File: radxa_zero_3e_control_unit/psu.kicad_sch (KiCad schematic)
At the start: 17 parts, among them J1 USB STM32, J11 ETH_IN, J12 ETH_OUT, J2 DC IN, U1 TPS54202DDC, U4 DCDC_MP2315, U7 PoE->24V

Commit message: Various
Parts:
- added J26, J27: IO, Connector_JST:JST_XH_B6B-XH-A_1x06_P2.50mm_Vertical, symbol Connector_Generic:Conn_01x06
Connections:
- net +5V: now also J27.5 (Pin_5), J27.6 (Pin_6)
- net +9V: now also J27.1 (Pin_1), J27.2 (Pin_2)
- net 5-24V: now also J2.1, J26.1 (Pin_1), J26.2 (Pin_2), J26.3 (Pin_3); no longer J2.2
- net GND: now also J2.2, J2.3, J26.4 (Pin_4), J26.5 (Pin_5), J26.6 (Pin_6), J27.3 (Pin_3), J27.4 (Pin_4); no longer J2.1
- no-connect marks 14 -> 13

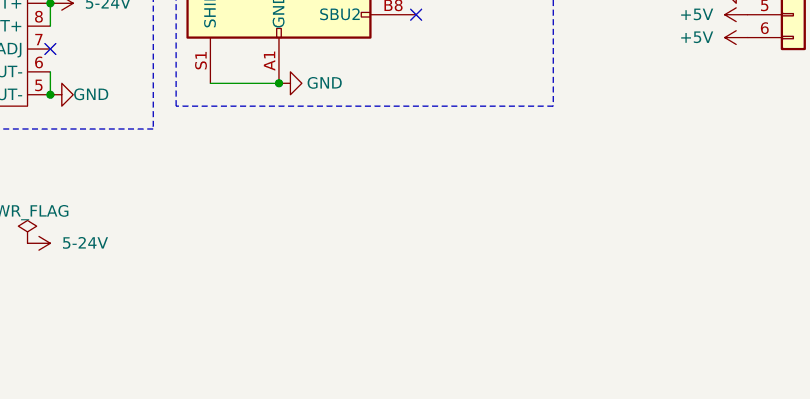
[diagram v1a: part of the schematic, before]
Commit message: WIP, before repinning SUM32G431
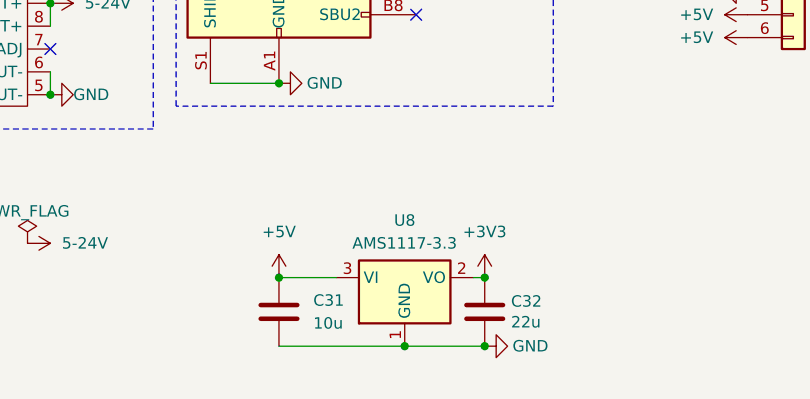
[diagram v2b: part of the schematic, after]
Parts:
- added C31: 10u, Capacitor_SMD:C_0805_2012Metric_Pad1.18x1.45mm_HandSolder, symbol Device:C
- added C32: 22u, Capacitor_SMD:C_0805_2012Metric, symbol Device:C
- added U8: AMS1117-3.3, Package_TO_SOT_SMD:SOT-223-3_TabPin2, symbol Regulator_Linear:AMS1117-3.3
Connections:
- net +5V: now also C31.1, U8.3 (VI)
- net GND: now also C31.2, C32.2, U8.1 (GND)
- new net +3V3: C32.1, U8.2 (VO)

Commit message: Udated control unit pcb
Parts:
- removed J11: ETH_IN, liebler_CONN:RJ45_WithoutMagneticsTHT, symbol Connector:8P8C_Shielded
- removed J12: ETH_OUT, liebler_CONN:RJ45_WithoutMagneticsTHT, symbol Connector:8P8C_Shielded
- removed J26, J27: IO, Connector_JST:JST_XH_B6B-XH-A_1x06_P2.50mm_Vertical, symbol Connector_Generic:Conn_01x06
- removed U7: PoE->24V, liebler_MODULES:XC7010_DCDC_ISOLATED_MODUEL, symbol liebler_MODULES:XC7010_MODULE
- added X2: MT3608, liebler_MODULES:DCDC_MT3608, symbol liebler_MODULES:XL_4015
- C31: footprint Capacitor_SMD:C_0805_2012Metric_Pad1.18x1.45mm_HandSolder -> Capacitor_SMD:C_0805_2012Metric
- R3: footprint Resistor_SMD:R_0201_0603Metric -> Resistor_SMD:R_0402_1005Metric
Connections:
- net 5-24V: now also X2.1 (In+)
- net GND: now also X2.2 (In-), X2.3 (out-)
- new net +24V: X2.4 (out+)
- no-connect marks 13 -> 8
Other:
- note removed: "PoE->24V"
- note removed: "PoE-Splitter"

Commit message: Sigmoid Stepper
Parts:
- added C44: u1, Capacitor_SMD:C_0402_1005Metric, symbol Device:C
- added R37: R, Resistor_SMD:R_2010_5025Metric, symbol Device:R
- added U9: INA226, Package_SO:VSSOP-10_3x3mm_P0.5mm, symbol Sensor_Energy:INA226
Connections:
- net +3V3: now also C44.1, U9.6 (VS)
- net 5-24V: now also R37.2, U9.9 (Vin-); no longer J1.A4 (VBUS), J1.A9 (VBUS), J1.B4 (VBUS), J1.B9 (VBUS), J2.1
- net GND: now also C44.2, U9.1 (A1), U9.2 (A0), U9.7 (GND)
- new net +VDC: J1.A4 (VBUS), J1.A9 (VBUS), J1.B4 (VBUS), J1.B9 (VBUS), J2.1, R37.1, U9.10 (Vin+), U9.8 (Vbus)
- new net I2C3_SCL: U9.5 (SCL)
- new net I2C3_SDA: U9.4 (SDA)
